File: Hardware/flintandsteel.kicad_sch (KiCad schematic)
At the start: 37 parts, among them J1 RBUS, U1 ESP32-S3, Y1 40MHz±10ppm

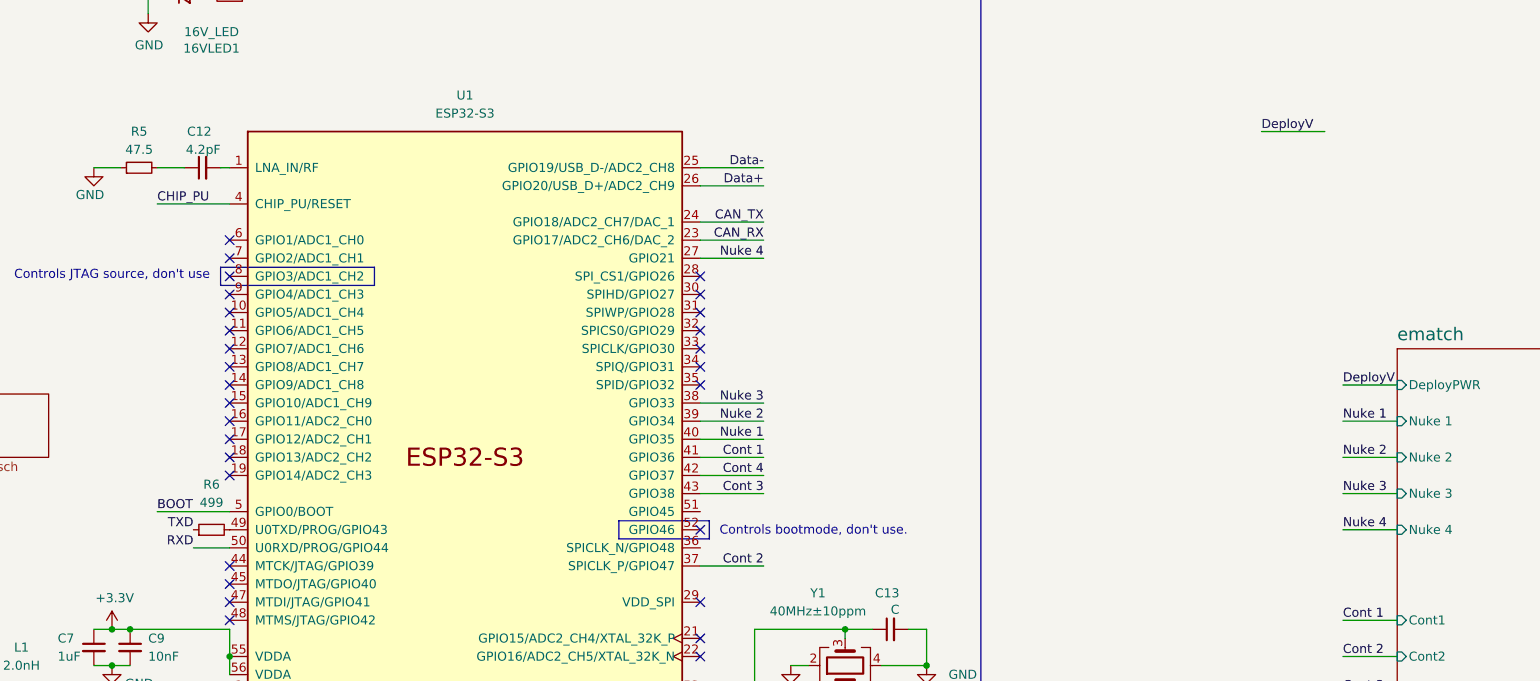
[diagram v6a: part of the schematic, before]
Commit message: removed can caps, better via stitching, fini?
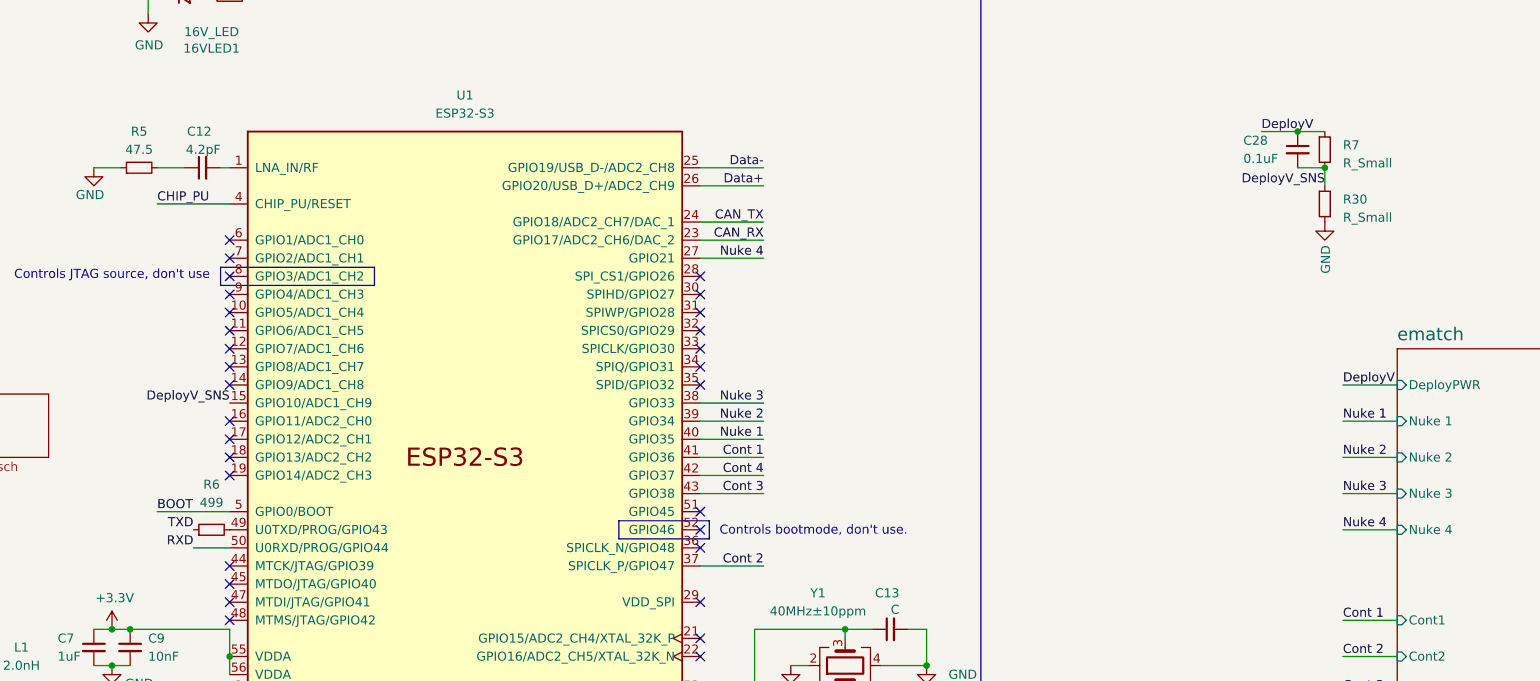
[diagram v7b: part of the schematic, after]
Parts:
- added C28: 0.1uF, Capacitor_SMD:C_0402_1005Metric, symbol Device:C_Small
- added R30, R7: R_Small, Resistor_SMD:R_0402_1005Metric, symbol Device:R_Small
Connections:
- net DeployV: now also C28.1, R7.1
- net GND: now also R30.2
- net DeployV_SNS: now reaches U1.15 (GPIO10/ADC1_CH9)
- net DeployV_SNS: now also C28.2, R30.1, R7.2
- no-connect marks 29 -> 30
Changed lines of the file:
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@@
   (junction (at 69.85 142.24) (diameter 0) (color 0 0 0 0)
   )
+  (junction (at 219.71 57.15) (diameter 0) (color 0 0 0 0)
+  )
   (junction (at 55.88 127) (diameter 0) (color 0 0 0 0)
   )
@@
   )
   (junction (at 16.51 170.18) (diameter 0) (color 0 0 0 0)
+  )
+  (junction (at 223.52 62.23) (diameter 0) (color 0 0 0 0)
   )
   (junction (at 270.51 33.02) (diameter 0) (color 0 0 0 0)
@@
   (no_connect (at 69.85 102.87))
   (no_connect (at 135.89 77.47))
+  (no_connect (at 135.89 115.57))
   (no_connect (at 69.85 90.17))
   (no_connect (at 69.85 72.39))
@@
   (no_connect (at 69.85 77.47))
   (no_connect (at 69.85 82.55))
-  (no_connect (at 69.85 95.25))
   (no_connect (at 69.85 80.01))
   (no_connect (at 69.85 120.65))
@@
   (no_connect (at 135.89 90.17))
   (no_connect (at 135.89 85.09))
+  (no_connect (at 135.89 110.49))
   (no_connect (at 69.85 118.11))
   (no_connect (at 135.89 123.19))
@@
     (stroke (width 0) (type default))
   )
+  (wire (pts (xy 219.71 57.15) (xy 223.52 57.15))
+    (stroke (width 0) (type default))
+  )
   (polyline (pts (xy 124.46 111.76) (xy 124.46 114.3))
     (stroke (width 0) (type default))
@@
     (stroke (width 0) (type default))
   )
+  (wire (pts (xy 223.52 62.23) (xy 223.52 64.77))
+    (stroke (width 0) (type default))
+  )
   (wire (pts (xy 144.78 118.11) (xy 135.89 118.11))
     (stroke (width 0) (type default))
@@
     (stroke (width 0) (type default))
   )
+  (wire (pts (xy 219.71 62.23) (xy 223.52 62.23))
+    (stroke (width 0) (type default))
+  )
   (wire (pts (xy 20.32 135.89) (xy 29.21 135.89))
     (stroke (width 0) (type default))
@@
     (stroke (width 0) (type default))
   )
-  (wire (pts (xy 214.63 57.15) (xy 223.52 57.15))
+  (wire (pts (xy 214.63 57.15) (xy 219.71 57.15))
     (stroke (width 0) (type default))
   )
@@
     (effects (font (size 1.27 1.27)) (justify left bottom))
   )
+  (label "DeployV_SNS" (at 223.52 64.77 180) (fields_autoplaced)
+    (effects (font (size 1.27 1.27)) (justify right bottom))
+  )
   (label "BOOT" (at 68.58 165.1 180) (fields_autoplaced)
     (effects (font (size 1.27 1.27)) (justify right bottom))
@@
   )
   (label "Cont 3" (at 144.78 107.95 180) (fields_autoplaced)
+    (effects (font (size 1.27 1.27)) (justify right bottom))
+  )
+  (label "DeployV_SNS" (at 69.85 95.25 180) (fields_autoplaced)
     (effects (font (size 1.27 1.27)) (justify right bottom))
   )
@@
     )
   )
+  (symbol (lib_id "Device:R_Small") (at 223.52 59.69 0) (unit 1)
+    (in_bom yes) (on_board yes) (dnp no) (fields_autoplaced)
+    (property "Reference" "R7" (at 226.06 59.055 0)
+      (effects (font (size 1.27 1.27)) (justify left))
+    )
+    (property "Value" "R_Small" (at 226.06 61.595 0)
+      (effects (font (size 1.27 1.27)) (justify left))
+    )
+    (property "Footprint" "Resistor_SMD:R_0402_1005Metric" (at 223.52 59.69 0)
+      (effects (font (size 1.27 1.27)) hide)
+    )
+    (property "Datasheet" "~" (at 223.52 59.69 0)
+      (effects (font (size 1.27 1.27)) hide)
+    )
+    (pin "1")
+    (pin "2")
+    (instances
+      (project "flintandsteel"
+        (path "/7db990e4-92e1-4f99-b4d2-435bbec1ba83"
+          (reference "R7") (unit 1)
+        )
+      )
+    )
+  )
   (symbol (lib_id "Connector:TestPoint") (at 29.21 38.1 90) (unit 1)
     (in_bom yes) (on_board yes) (dnp no)
@@
     )
   )
+  (symbol (lib_id "power:GND") (at 223.52 69.85 0) (unit 1)
+    (in_bom yes) (on_board yes) (dnp no)
+    (property "Reference" "#PWR015" (at 223.52 76.2 0)
+      (effects (font (size 1.27 1.27)) hide)
+    )
+    (property "Value" "GND" (at 223.647 73.1012 90)
+      (effects (font (size 1.27 1.27)) (justify right))
+    )
+    (property "Footprint" "" (at 223.52 69.85 0)
+      (effects (font (size 1.27 1.27)) hide)
+    )
+    (property "Datasheet" "" (at 223.52 69.85 0)
+      (effects (font (size 1.27 1.27)) hide)
+    )
+    (pin "1")
+    (instances
+      (project "flintandsteel"
+        (path "/7db990e4-92e1-4f99-b4d2-435bbec1ba83"
+          (reference "#PWR015") (unit 1)
+        )
+      )
+    )
+  )
   (symbol (lib_id "Device:C_Small") (at 50.8 129.54 0) (unit 1)
     (in_bom yes) (on_board yes) (dnp no)
@@
         (path "/7db990e4-92e1-4f99-b4d2-435bbec1ba83"
           (reference "#PWR014") (unit 1)
+        )
+      )
+    )
+  )
+  (symbol (lib_id "Device:R_Small") (at 223.52 67.31 0) (unit 1)
+    (in_bom yes) (on_board yes) (dnp no) (fields_autoplaced)
+    (property "Reference" "R30" (at 226.06 66.675 0)
+      (effects (font (size 1.27 1.27)) (justify left))
+    )
+    (property "Value" "R_Small" (at 226.06 69.215 0)
+      (effects (font (size 1.27 1.27)) (justify left))
+    )
+    (property "Footprint" "Resistor_SMD:R_0402_1005Metric" (at 223.52 67.31 0)
+      (effects (font (size 1.27 1.27)) hide)
+    )
+    (property "Datasheet" "~" (at 223.52 67.31 0)
+      (effects (font (size 1.27 1.27)) hide)
+    )
+    (pin "1")
+    (pin "2")
+    (instances
+      (project "flintandsteel"
+        (path "/7db990e4-92e1-4f99-b4d2-435bbec1ba83"
+          (reference "R30") (unit 1)
         )
       )
@@
         )
       )
+    )
+  )
+  (symbol (lib_id "Device:C_Small") (at 219.71 59.69 0) (unit 1)
+    (in_bom yes) (on_board yes) (dnp no)
+    (property "Reference" "C28" (at 212.09 58.42 0)
+      (effects (font (size 1.27 1.27)) (justify left))
+    )
+    (property "Value" "0.1uF" (at 212.09 60.96 0)
+      (effects (font (size 1.27 1.27)) (justify left))
+    )
+    (property "Footprint" "Capacitor_SMD:C_0402_1005Metric" (at 219.71 59.69 0)
+      (effects (font (size 1.27 1.27)) hide)
+    )
+    (property "Datasheet" "~" (at 219.71 59.69 0)
+      (effects (font (size 1.27 1.27)) hide)
+    )
+    (pin "1")
+    (pin "2")
+    (instances
+      (project "flintandsteel"
+        (path "/7db990e4-92e1-4f99-b4d2-435bbec1ba83"
+          (reference "C28") (unit 1)
+        )
+      )

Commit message: Kiran's review
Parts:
- C12: value 4.2pF -> DNP
- C13, C14: value C -> 11pF
- R30: value R_Small -> 10k
- R5: value 47.5 -> DNP
- R7: value R_Small -> 124k
- Y1: value 40MHz±10ppm -> R940000171
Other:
- sheet ematch renamed Pyro
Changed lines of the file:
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@@
     (stroke (width 0) (type default))
+  )
+  (text_box "Crystal must be 40 MHz and at least ±10ppm"
+    (at 144.78 139.7 0) (size 19.05 11.43)
+    (stroke (width -0.0001) (type default))
+    (fill (type none))
+    (effects (font (size 1.27 1.27)) (justify left top))
   )
   (text "Controls bootmode, don't use.\n" (at 138.5894 113.9757 0)
@@
       (effects (font (size 1.27 1.27)) (justify left))
     )
-    (property "Value" "R_Small" (at 226.06 61.595 0)
+    (property "Value" "124k" (at 226.06 61.595 0)
       (effects (font (size 1.27 1.27)) (justify left))
     )
@@
       (effects (font (size 1.27 1.27)) (justify left))
     )
-    (property "Value" "R_Small" (at 226.06 69.215 0)
+    (property "Value" "10k" (at 226.06 69.215 0)
       (effects (font (size 1.27 1.27)) (justify left))
     )
@@
       (effects (font (size 1.27 1.27)) (justify left))
     )
-    (property "Value" "C" (at 165.1 144.5514 90)
+    (property "Value" "11pF" (at 165.1 144.5514 90)
       (effects (font (size 1.27 1.27)) (justify left))
     )
@@
   (symbol (lib_id "Device:C_Small") (at 162.56 127 90) (unit 1)
     (in_bom yes) (on_board yes) (dnp no)
-    (property "Reference" "C13" (at 163.83 121.92 90)
-      (effects (font (size 1.27 1.27)) (justify left))
-    )
-    (property "Value" "C" (at 163.83 124.2314 90)
+    (property "Reference" "C13" (at 165.1 121.92 90)
+      (effects (font (size 1.27 1.27)) (justify left))
+    )
+    (property "Value" "11pF" (at 165.1 124.2314 90)
       (effects (font (size 1.27 1.27)) (justify left))
     )
@@
       (effects (font (size 1.27 1.27)) (justify left))
     )
-    (property "Value" "4.2pF" (at 68.58 59.69 90)
+    (property "Value" "DNP" (at 68.58 59.69 90)
       (effects (font (size 1.27 1.27)) (justify left))
     )
@@
       (effects (font (size 1.27 1.27)))
     )
-    (property "Value" "40MHz±10ppm" (at 152.4 124.46 90)
+    (property "Value" "R940000171" (at 152.4 124.46 90)
       (effects (font (size 1.27 1.27)))
     )
@@
       (effects (font (size 1.27 1.27)))
     )
-    (property "Value" "47.5" (at 57.15 59.69 90)
+    (property "Value" "DNP" (at 57.15 59.69 90)
       (effects (font (size 1.27 1.27)))
     )
@@
     (stroke (width 0) (type solid))
     (fill (color 0 0 0 0.0000))
-    (property "Sheetname" "ematch" (at 233.68 86.6517 0)
+    (property "Sheetname" "Pyro" (at 233.68 86.6517 0)
       (effects (font (size 1.8034 1.8034)) (justify left bottom))
     )
